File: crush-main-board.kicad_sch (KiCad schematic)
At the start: 25 parts, among them J1 4x4_Header, J10 3x3 Header, J11 3x3 Header, J12 3x2 Header, J13 3x4_Header, J14 3x4_Header, J15 2157601008, J2 4x4_Header, J3 6x2_Header, J4 3x1_Header, J5 3x2 Header, J6 3x2 Header, J7 3x4 Header, J8 3x4 Header, J9 3x3 Header, U1 Teensy4.1, U2 ISO7740DW, U3 ISO7740DW

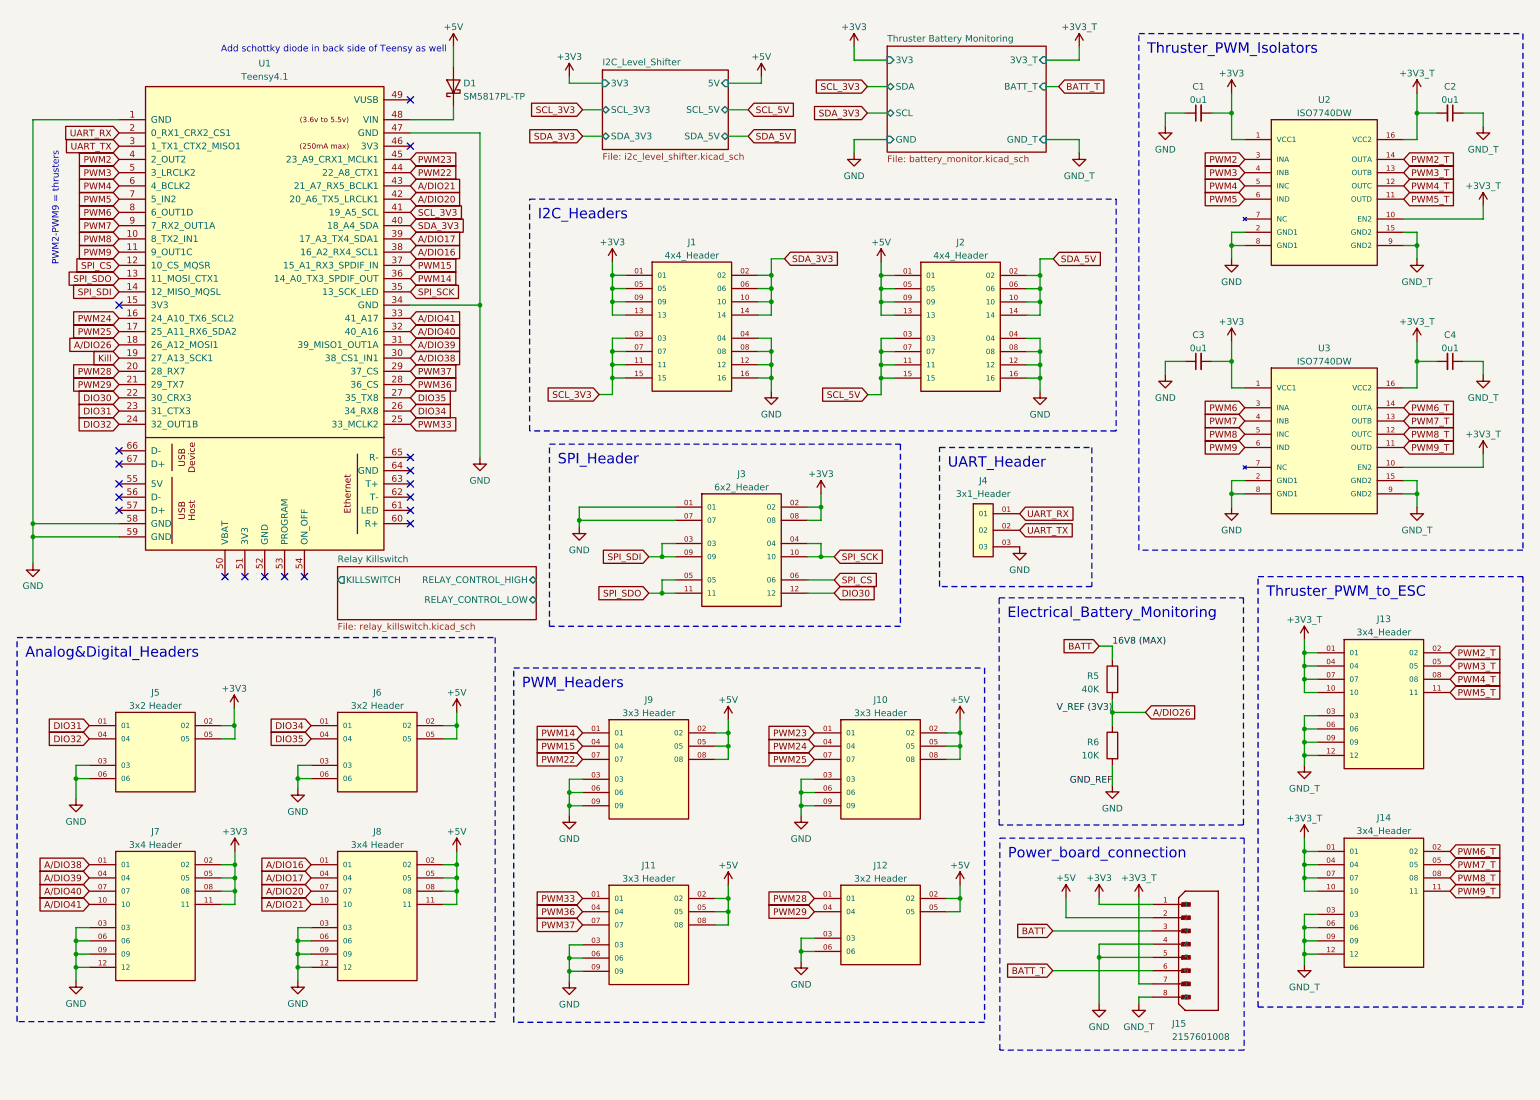
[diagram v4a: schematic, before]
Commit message: Switch to INA232
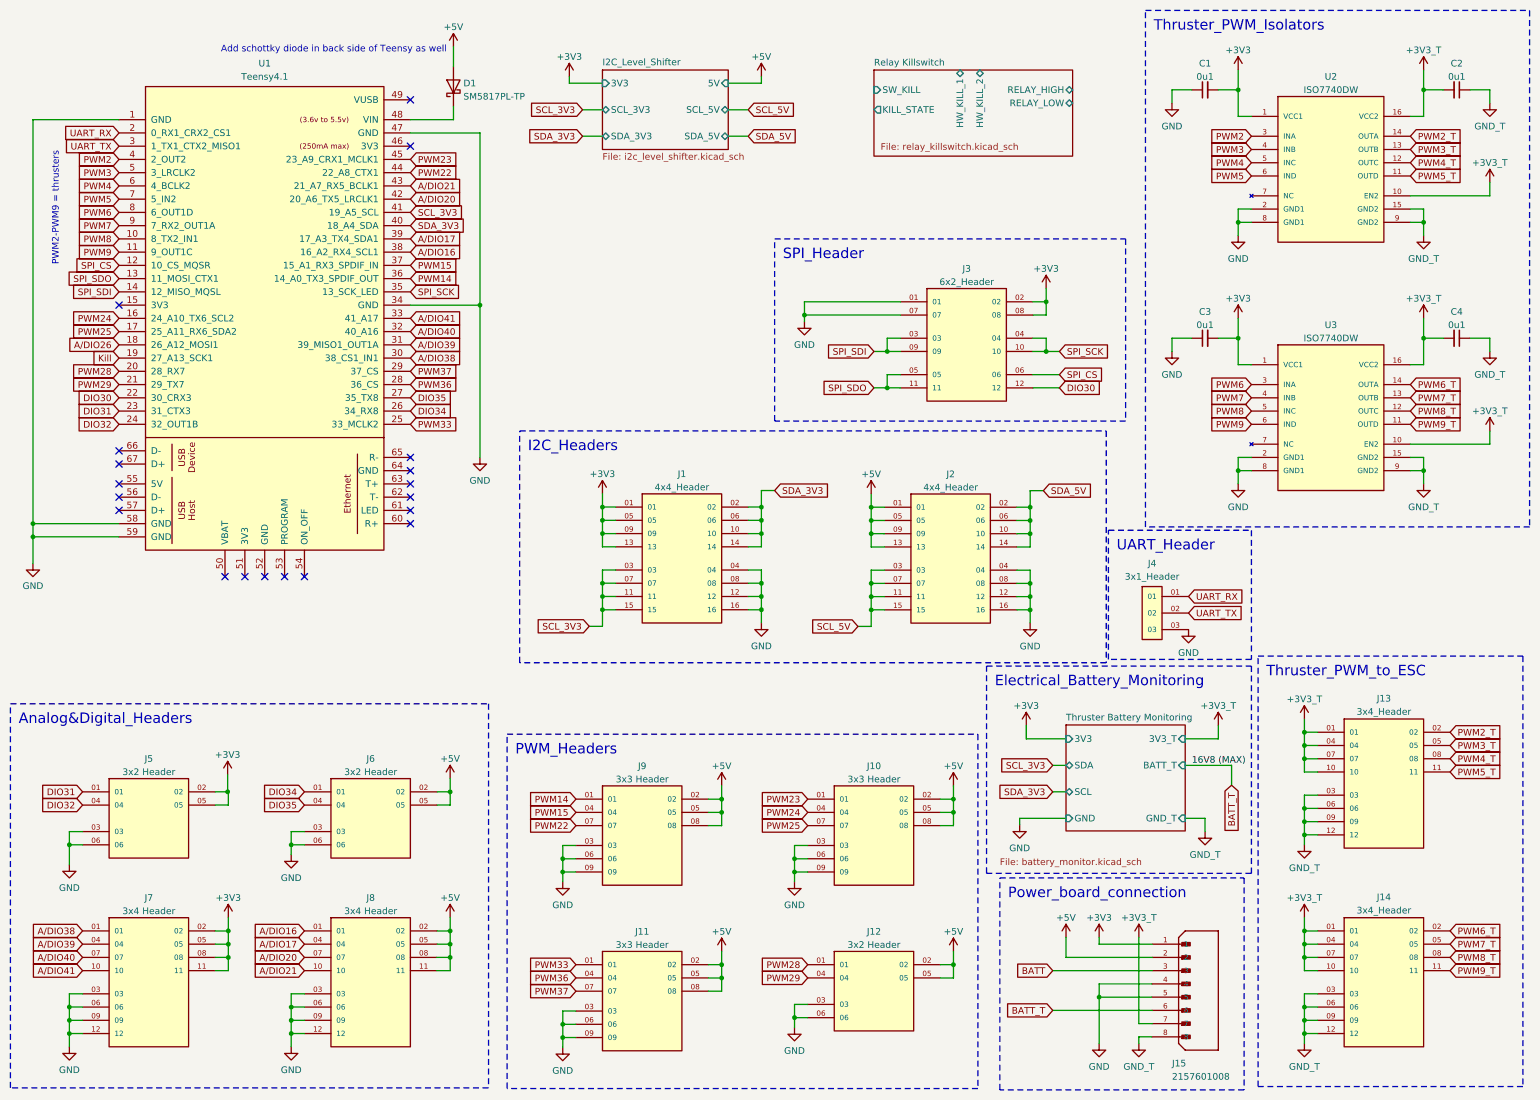
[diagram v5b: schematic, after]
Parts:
- removed R5: 40K, Resistor_SMD:R_0603_1608Metric_Pad0.98x0.95mm_HandSolder, symbol Device:R
- removed R6: 10K, Resistor_SMD:R_0603_1608Metric_Pad0.98x0.95mm_HandSolder, symbol Device:R
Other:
- sheet Relay Killswitch ports: added HW_KILL_1, HW_KILL_2, KILL_STATE, RELAY_HIGH, RELAY_LOW, SW_KILL; removed KILLSWITCH, RELAY_CONTROL_HIGH, RELAY_CONTROL_LOW
- moved on the sheet: C1, C2, C3, C4, J1, J10, J11, J12, J13, J14, J15, J2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

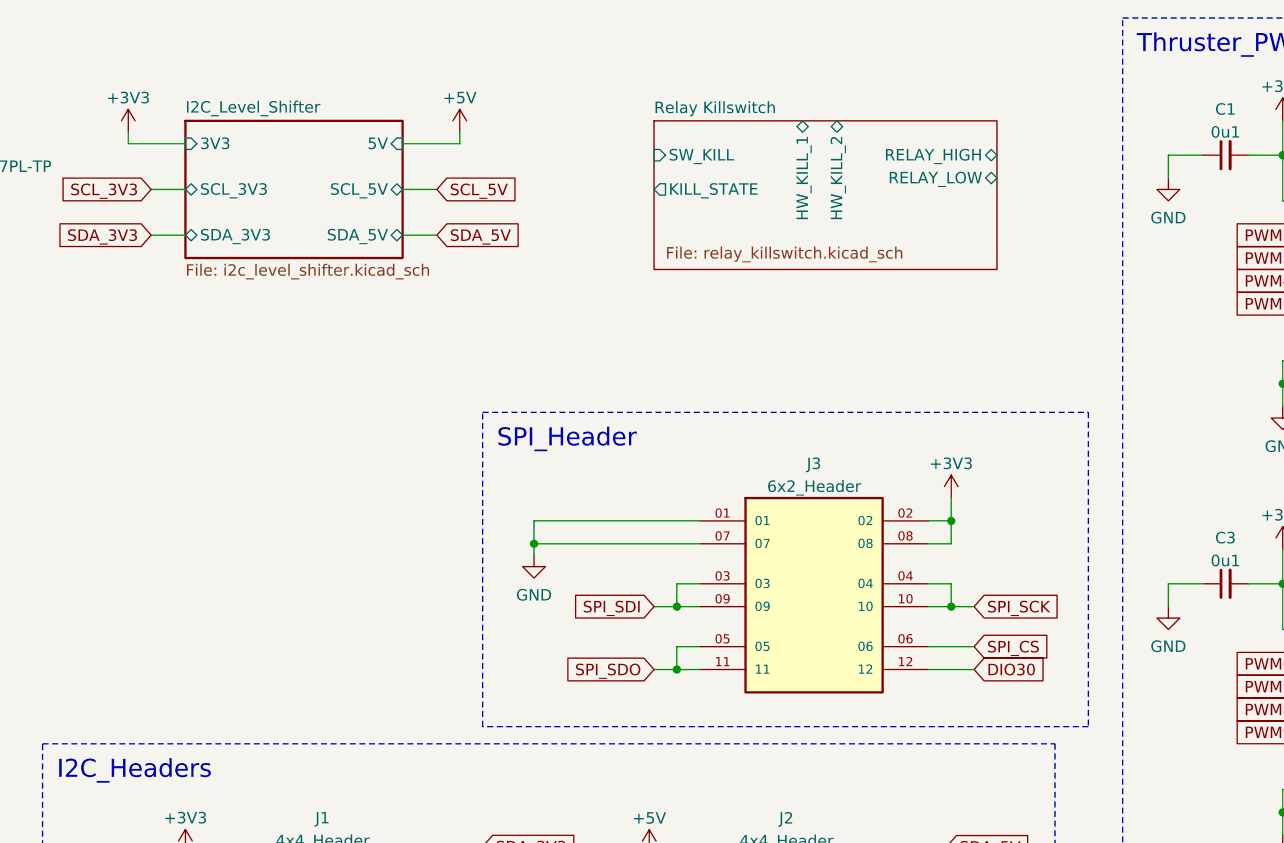
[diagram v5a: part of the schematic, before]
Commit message: Wire up the relay killswitch with JSTs
In the schematic
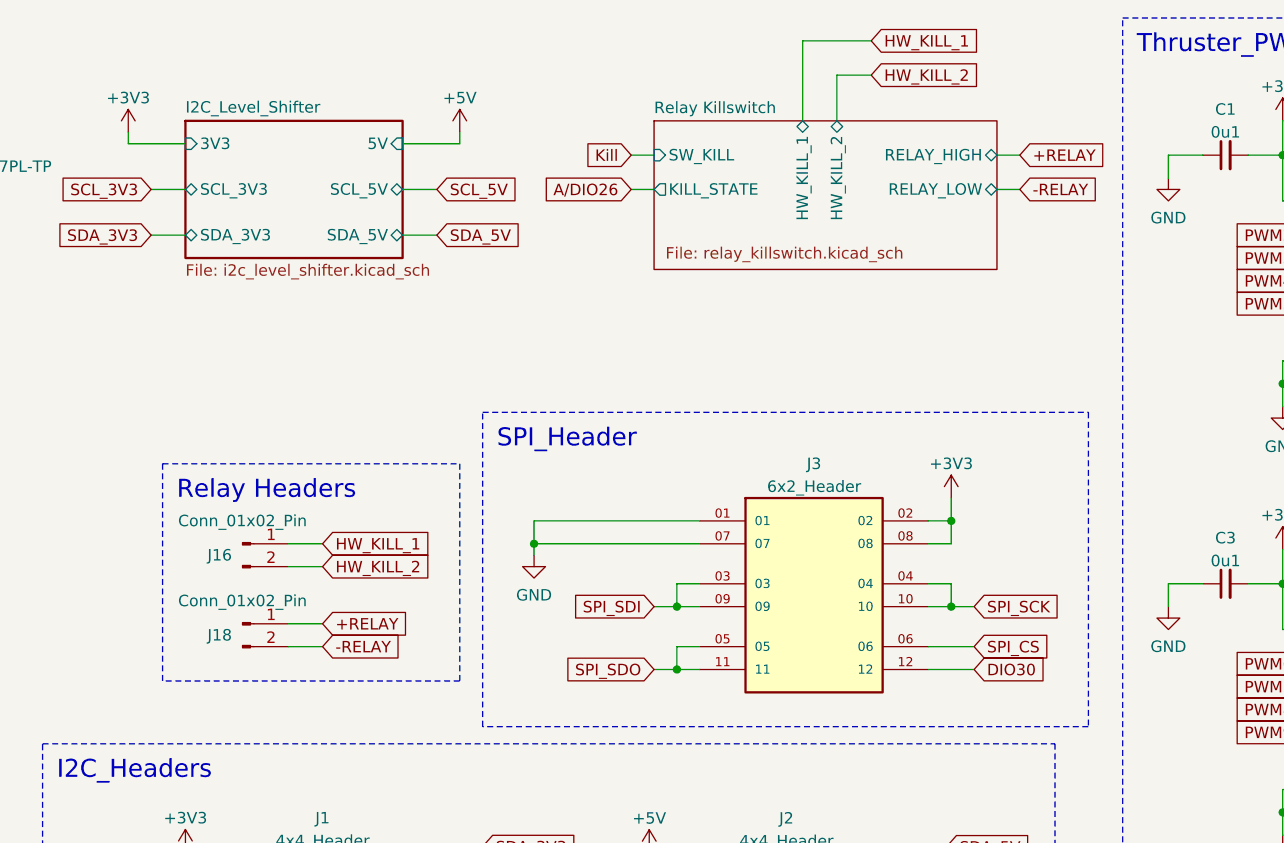
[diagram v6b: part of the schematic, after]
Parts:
- added J16, J18: Conn_01x02_Pin, Connector_JST:JST_XH_S2B-XH-A_1x02_P2.50mm_Horizontal, symbol Connector:Conn_01x02_Pin
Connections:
- new net +RELAY: J18.1 (Pin_1)
- new net -RELAY: J18.2 (Pin_2)
- new net HW_KILL_1: J16.1 (Pin_1)
- new net HW_KILL_2: J16.2 (Pin_2)
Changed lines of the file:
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@@
     (stroke (width 0) (type default))
   )
+  (wire (pts (xy 127 63.5) (xy 130.81 63.5))
+    (stroke (width 0) (type default))
+  )
   (wire (pts (xy 167.1066 95.2754) (xy 167.1066 97.8154))
     (stroke (width 0) (type default))
@@
     (stroke (width 0) (type default))
   )
+  (wire (pts (xy 127 60.96) (xy 130.81 60.96))
+    (stroke (width 0) (type default))
+  )
   (wire (pts (xy 138.43 188.087) (xy 138.43 190.627))
     (stroke (width 0) (type default))
@@
     (stroke (width 0) (type default))
   )
+  (wire (pts (xy 208.28 21.59) (xy 205.74 21.59))
+    (stroke (width 0) (type default))
+  )
   (wire (pts (xy 86.36 186.69) (xy 83.82 186.69))
     (stroke (width 0) (type default))
@@
     (stroke (width 0) (type default))
   )
+  (wire (pts (xy 165.1 17.78) (xy 167.64 17.78))
+    (stroke (width 0) (type default))
+  )
   (wire (pts (xy 197.5866 117.5004) (xy 195.0466 117.5004))
     (stroke (width 0) (type default))
@@
     (stroke (width 0) (type default))
   )
+  (wire (pts (xy 205.74 17.78) (xy 208.28 17.78))
+    (stroke (width 0) (type default))
+  )
   (wire (pts (xy 250.19 191.135) (xy 250.19 193.675))
     (stroke (width 0) (type default))
   )
+  (wire (pts (xy 184.15 5.08) (xy 184.15 13.97))
+    (stroke (width 0) (type default))
+  )
   (wire (pts (xy 237.49 88.265) (xy 237.49 90.805))
     (stroke (width 0) (type default))
@@
     (stroke (width 0) (type default))
   )
+  (wire (pts (xy 191.77 8.89) (xy 187.96 8.89))
+    (stroke (width 0) (type default))
+  )
   (wire (pts (xy 220.98 189.23) (xy 210.82 189.23))
     (stroke (width 0) (type default))
@@
     (stroke (width 0) (type default))
   )
+  (wire (pts (xy 165.1 21.59) (xy 167.64 21.59))
+    (stroke (width 0) (type default))
+  )
   (wire (pts (xy 273.05 90.805) (xy 273.05 93.345))
     (stroke (width 0) (type default))
@@
     (stroke (width 0) (type default))
   )
+  (wire (pts (xy 187.96 8.89) (xy 187.96 13.97))
+    (stroke (width 0) (type default))
+  )
   (wire (pts (xy 273.05 43.18) (xy 273.05 45.72))
     (stroke (width 0) (type default))
@@
     (stroke (width 0) (type default))
   )
+  (wire (pts (xy 127 72.39) (xy 130.81 72.39))
+    (stroke (width 0) (type default))
+  )
   (wire (pts (xy 138.43 151.257) (xy 138.43 153.797))
     (stroke (width 0) (type default))
@@
     (stroke (width 0) (type default))
   )
+  (wire (pts (xy 191.77 5.08) (xy 184.15 5.08))
+    (stroke (width 0) (type default))
+  )
   (wire (pts (xy 13.335 160.02) (xy 13.335 162.56))
     (stroke (width 0) (type default))
@@
     (stroke (width 0) (type default))
   )
+  (wire (pts (xy 127 69.85) (xy 130.81 69.85))
+    (stroke (width 0) (type default))
+  )
   (wire (pts (xy 273.05 61.595) (xy 273.05 65.405))
     (stroke (width 0) (type default))
@@
     (effects (font (size 2 2)) (justify left top))
   )
+  (text_box "Relay Headers"
+    (at 113.03 52.07 0) (size 33.02 24.13)
+    (stroke (width 0) (type dash))
+    (fill (type none))
+    (effects (font (size 2 2)) (justify left top))
+  )
   (text_box "Electrical_Battery_Monitoring\n"
     (at 189.23 128.27 0) (size 50.8 39.751)
@@
     )
   )
+  (global_label "HW_KILL_1" (shape input) (at 191.77 5.08 0) (fields_autoplaced)
+    (effects (font (size 1.27 1.27)) (justify left))
+    (property "Intersheetrefs" "${INTERSHEET_REFS}" (at 204.5334 5.08 0)
+      (effects (font (size 1.27 1.27)) (justify left) hide)
+    )
+  )
+  (global_label "HW_KILL_2" (shape input) (at 130.81 63.5 0) (fields_autoplaced)
+    (effects (font (size 1.27 1.27)) (justify left))
+    (property "Intersheetrefs" "${INTERSHEET_REFS}" (at 143.5734 63.5 0)
+      (effects (font (size 1.27 1.27)) (justify left) hide)
+    )
+  )
   (global_label "PWM7" (shape input) (at 240.03 76.835 180) (fields_autoplaced)
     (effects (font (size 1.27 1.27)) (justify right))
@@
     )
   )
+  (global_label "-RELAY" (shape input) (at 208.28 21.59 0) (fields_autoplaced)
+    (effects (font (size 1.27 1.27)) (justify left))
+    (property "Intersheetrefs" "${INTERSHEET_REFS}" (at 218.3825 21.59 0)
+      (effects (font (size 1.27 1.27)) (justify left) hide)
+    )
+  )
   (global_label "PWM29" (shape input) (at 22.86 74.295 180) (fields_autoplaced)
     (effects (font (size 1.27 1.27)) (justify right))
@@
     )
   )
+  (global_label "-RELAY" (shape input) (at 130.81 72.39 0) (fields_autoplaced)
+    (effects (font (size 1.27 1.27)) (justify left))
+    (property "Intersheetrefs" "${INTERSHEET_REFS}" (at 140.9125 72.39 0)
+      (effects (font (size 1.27 1.27)) (justify left) hide)
+    )
+  )
   (global_label "PWM8" (shape input) (at 22.86 46.355 180) (fields_autoplaced)
     (effects (font (size 1.27 1.27)) (justify right))
@@
     )
   )
+  (global_label "HW_KILL_1" (shape input) (at 130.81 60.96 0) (fields_autoplaced)
+    (effects (font (size 1.27 1.27)) (justify left))
+    (property "Intersheetrefs" "${INTERSHEET_REFS}" (at 143.5734 60.96 0)
+      (effects (font (size 1.27 1.27)) (justify left) hide)
+    )
+  )
   (global_label "DIO35" (shape input) (at 78.74 76.835 0) (fields_autoplaced)
     (effects (font (size 1.27 1.27)) (justify left))
@@
     )
   )
+  (global_label "+RELAY" (shape input) (at 208.28 17.78 0) (fields_autoplaced)
+    (effects (font (size 1.27 1.27)) (justify left))
+    (property "Intersheetrefs" "${INTERSHEET_REFS}" (at 218.3825 17.78 0)
+      (effects (font (size 1.27 1.27)) (justify left) hide)
+    )
+  )
   (global_label "SDA_5V" (shape input) (at 143.51 26.67 0) (fields_autoplaced)
     (effects (font (size 1.27 1.27)) (justify left))
@@
     )
   )
+  (global_label "Kill" (shape input) (at 165.1 17.78 180) (fields_autoplaced)
+    (effects (font (size 1.27 1.27)) (justify right))
+    (property "Intersheetrefs" "${INTERSHEET_REFS}" (at 158.989 17.78 0)
+      (effects (font (size 1.27 1.27)) (justify right) hide)
+    )
+  )
   (global_label "A{slash}DIO16" (shape input) (at 58.42 179.07 180) (fields_autoplaced)
     (effects (font (size 1.27 1.27)) (justify right))
@@
     )
   )
+  (global_label "+RELAY" (shape input) (at 130.81 69.85 0) (fields_autoplaced)
+    (effects (font (size 1.27 1.27)) (justify left))
+    (property "Intersheetrefs" "${INTERSHEET_REFS}" (at 140.9125 69.85 0)
+      (effects (font (size 1.27 1.27)) (justify left) hide)
+    )
+  )
   (global_label "SCL_3V3" (shape input) (at 78.74 41.275 0) (fields_autoplaced)
     (effects (font (size 1.27 1.27)) (justify left))
@@
     )
   )
+  (global_label "HW_KILL_2" (shape input) (at 191.77 8.89 0) (fields_autoplaced)
+    (effects (font (size 1.27 1.27)) (justify left))
+    (property "Intersheetrefs" "${INTERSHEET_REFS}" (at 204.5334 8.89 0)
+      (effects (font (size 1.27 1.27)) (justify left) hide)
+    )
+  )
   (global_label "PWM23" (shape input) (at 78.74 31.115 0) (fields_autoplaced)
     (effects (font (size 1.27 1.27)) (justify left))
@@
     )
   )
+  (global_label "A{slash}DIO26" (shape input) (at 165.1 21.59 180) (fields_autoplaced)
+    (effects (font (size 1.27 1.27)) (justify right))
+    (property "Intersheetrefs" "${INTERSHEET_REFS}" (at 154.1508 21.59 0)
+      (effects (font (size 1.27 1.27)) (justify right) hide)
+    )
+  )
   (global_label "PWM3_T" (shape input) (at 278.13 143.51 0) (fields_autoplaced)
     (effects (font (size 1.27 1.27)) (justify left))
@@
     )
   )
+  (symbol (lib_id "Connector:Conn_01x02_Pin") (at 121.92 60.96 0) (unit 1)
+    (in_bom yes) (on_board yes) (dnp no)
+    (property "Reference" "J16" (at 119.38 62.23 0)
+      (effects (font (size 1.27 1.27)))
+    )
+    (property "Value" "Conn_01x02_Pin" (at 121.92 58.42 0)
+      (effects (font (size 1.27 1.27)))
+    )
+    (property "Footprint" "Connector_JST:JST_XH_S2B-XH-A_1x02_P2.50mm_Horizontal" (at 121.92 60.96 0)
+      (effects (font (size 1.27 1.27)) hide)
+    )
+    (property "Datasheet" "~" (at 121.92 60.96 0)
+      (effects (font (size 1.27 1.27)) hide)
+    )
+    (pin "1")
+    (pin "2")
+    (instances
+      (project "crush-main-board"
+        (path "/74b566fe-9d71-4817-95ed-d472d647f8c8"
+          (reference "J16") (unit 1)
+        )
+      )
+    )
+  )
   (symbol (lib_id "power:GND") (at 55.88 201.295 0) (mirror y) (unit 1)
     (in_bom yes) (on_board yes) (dnp no)
@@
     )
   )
+  (symbol (lib_id "Connector:Conn_01x02_Pin") (at 121.92 69.85 0) (unit 1)
+    (in_bom yes) (on_board yes) (dnp no)
+    (property "Reference" "J18" (at 119.38 71.12 0)
+      (effects (font (size 1.27 1.27)))
+    )
+    (property "Value" "Conn_01x02_Pin" (at 121.92 67.31 0)
+      (effects (font (size 1.27 1.27)))
+    )
+    (property "Footprint" "Connector_JST:JST_XH_S2B-XH-A_1x02_P2.50mm_Horizontal" (at 121.92 69.85 0)
+      (effects (font (size 1.27 1.27)) hide)
+    )
+    (property "Datasheet" "~" (at 121.92 69.85 0)
+      (effects (font (size 1.27 1.27)) hide)
+    )
+    (pin "1")
+    (pin "2")
+    (instances
+      (project "crush-main-board"
+        (path "/74b566fe-9d71-4817-95ed-d472d647f8c8"
+          (reference "J18") (unit 1)
+        )
+      )
+    )
+  )
   (symbol (lib_id "power:GND") (at 224.79 20.32 0) (unit 1)
     (in_bom yes) (on_board yes) (dnp no)
@@
       (effects (font (size 1.27 1.27)) (justify right))
     )
-    (pin "RELAY_LOW" bidirectional (at 205.74 20.32 0)
+    (pin "RELAY_LOW" bidirectional (at 205.74 21.59 0)
       (effects (font (size 1.27 1.27)) (justify right))
     )

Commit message: Start laying out main board
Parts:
- removed J16, J18: Conn_01x02_Pin, Connector_JST:JST_XH_S2B-XH-A_1x02_P2.50mm_Horizontal, symbol Connector:Conn_01x02_Pin
- added J16, J17: Conn_01x02, Connector_PinHeader_2.54mm:PinHeader_1x02_P2.54mm_Vertical, symbol Connector_Generic:Conn_01x02
- J1: footprint Crush_Mainboard_Footprints:4x4_Header -> Crush_Mainboard_Footprints:3x1_Header
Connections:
- net +RELAY: now also J17.2 (Pin_2)
- net -RELAY: now also J17.1 (Pin_1)
- net HW_KILL_1: now also J16.2 (Pin_2)
- net HW_KILL_2: now also J16.1 (Pin_1)
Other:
- moved on the sheet: C1, C2, C3, C4, J1, J10, J11, J12, J13, J14, J15, J2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
